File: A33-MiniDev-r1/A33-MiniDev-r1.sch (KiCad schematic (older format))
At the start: 8 parts, among them IC1 AXP223, U1 A33

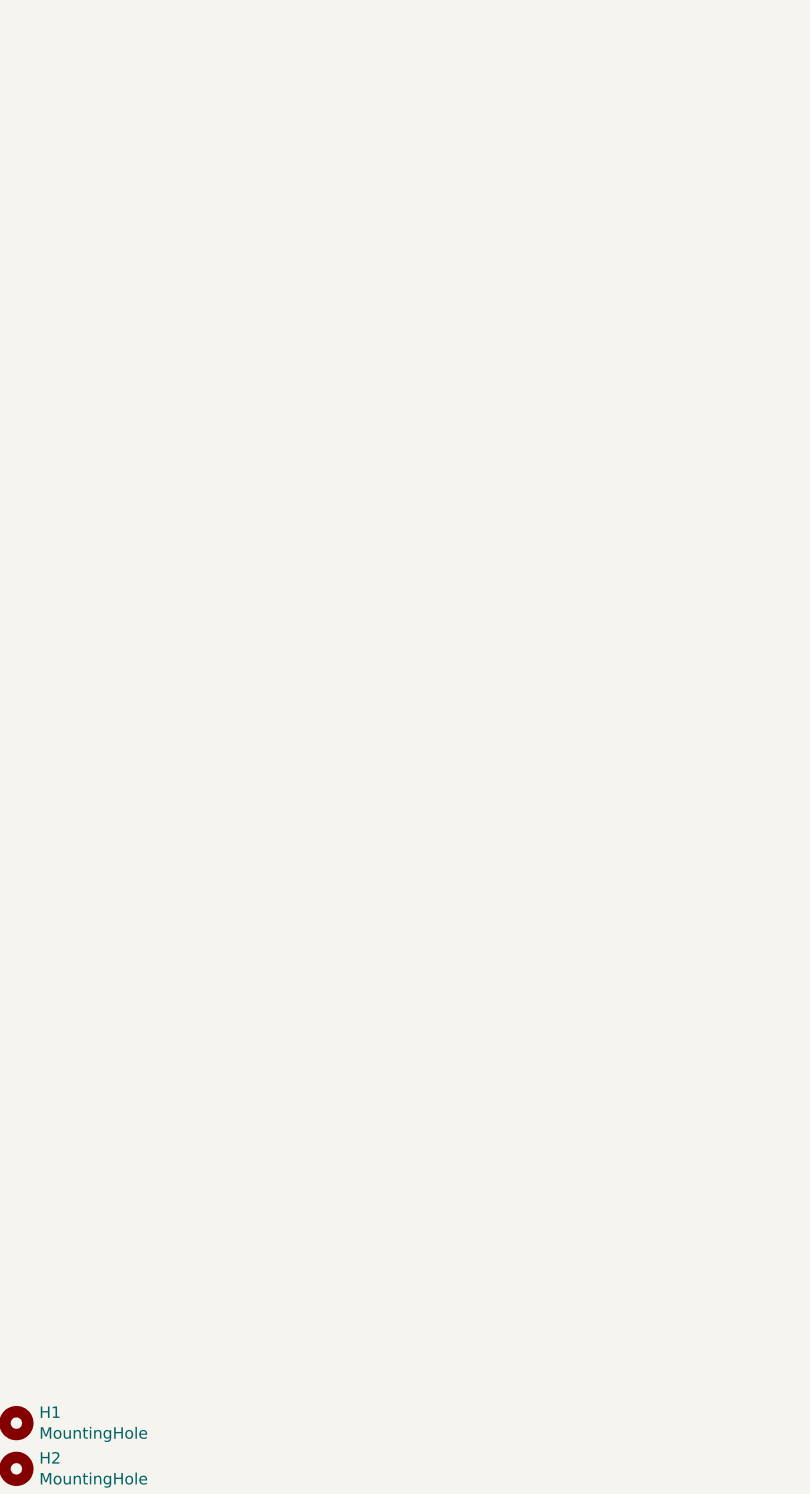
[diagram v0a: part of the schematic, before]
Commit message: Uploaded RAM chip library and placed on schematic
IS43TR16640CL-123JBLI
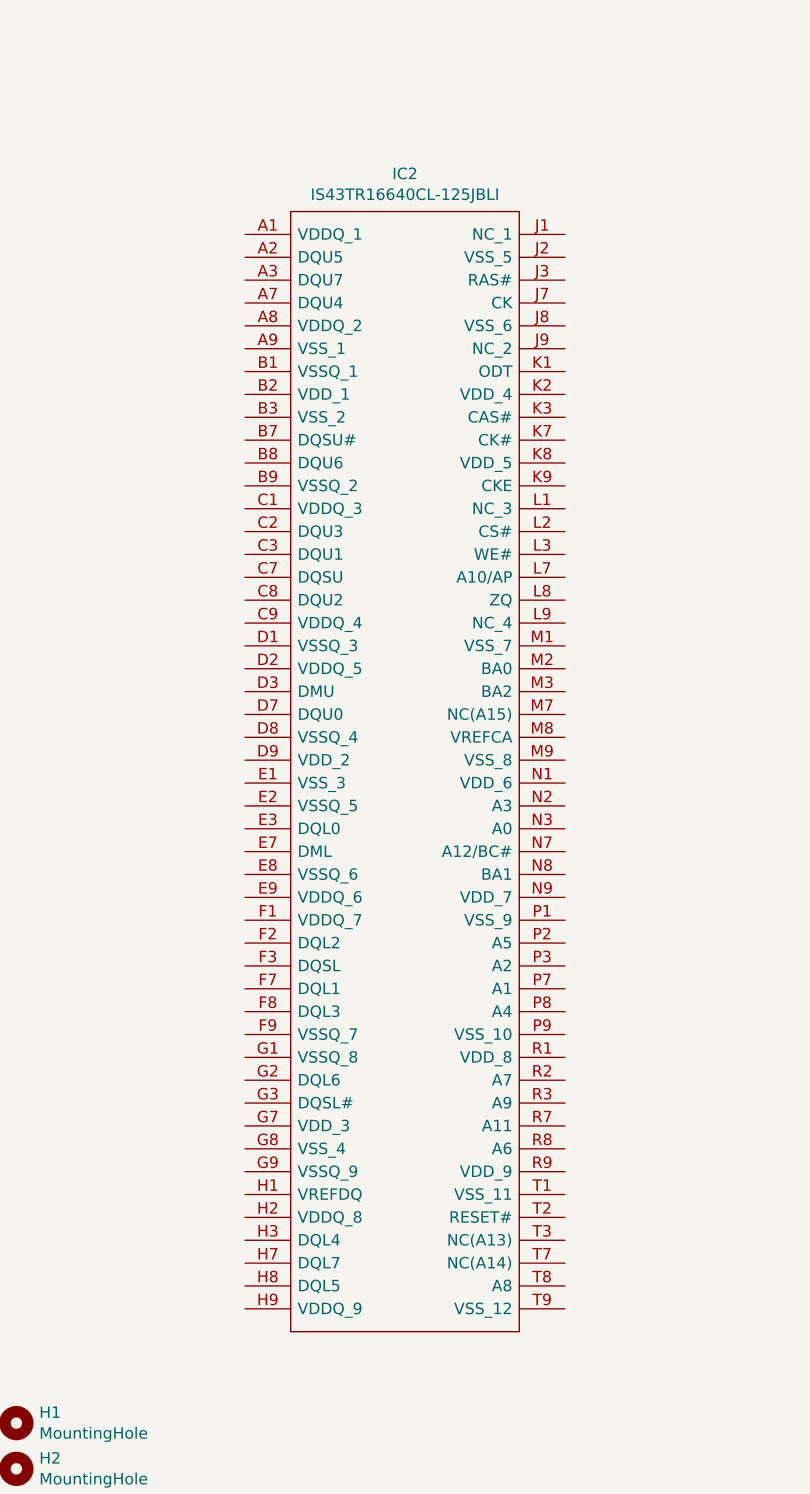
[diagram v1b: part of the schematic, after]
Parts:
- added IC2: IS43TR16640CL-125JBLI, BGA96C80P9X16_900X1300X120, symbol IS43TR16640CL-125JBLI:IS43TR16640CL-125JBLI
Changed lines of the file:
@@
 Wire Wire Line
 	16900 2100 16900 1900
-Wire Bus Line
-	3500 1600 3500 3100
 $Comp
 L power:VBUS 5V_EXT
@@
 	1    0    0    -1
 $EndComp
+Wire Bus Line
+	3500 1600 3500 3100
+$Comp
+L IS43TR16640CL-125JBLI:IS43TR16640CL-125JBLI IC2
+U 1 1 61103768
+P 2000 9800
+F 0 "IC2" H 2700 10065 50  0000 C CNN
+F 1 "IS43TR16640CL-125JBLI" H 2700 9974 50  0000 C CNN
+F 2 "BGA96C80P9X16_900X1300X120" H 3250 9900 50  0001 L CNN
+F 3 "https://www.issi.com/WW/pdf/43-46TR16640C-81280CL.pdf" H 3250 9800 50  0001 L CNN
+F 4 "DRAM 1G, 1.35V, DDR3, 64Mx16, 1600MT/s @ 10-10-10, 96 ball BGA (9mm x13mm) RoHS. IT" H 3250 9700 50  0001 L CNN "Description"
+F 5 "1.2" H 3250 9600 50  0001 L CNN "Height"
+F 6 "870-16640CL-125JBLI" H 3250 9500 50  0001 L CNN "Mouser Part Number"
+F 7 "https://www.mouser.co.uk/ProductDetail/ISSI/IS43TR16640CL-125JBLI?qs=BJlw7L4Cy7%2F%252B7noTMkJDFw%3D%3D" H 3250 9400 50  0001 L CNN "Mouser Price/Stock"
+F 8 "Integrated Silicon Solution Inc." H 3250 9300 50  0001 L CNN "Manufacturer_Name"
+F 9 "IS43TR16640CL-125JBLI" H 3250 9200 50  0001 L CNN "Manufacturer_Part_Number"
+	1    2000 9800
+	1    0    0    -1
+$EndComp

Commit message: Uploaded MOSFET; initial power connections on schematic
Caps and resistors not picked yet (hopefully in stock...) but RAM chips and MOSFETs have been ordered
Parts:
- added C? (x2): 1uF, symbol Device:C_Small
- added C?, Cx (x4): 10uF/6.3V, symbol Device:C_Small
- added Q1: CSD25310Q2T, CSD25310Q2T, symbol CSD25310Q2T:CSD25310Q2T
- added R1, R2: 22R, symbol Device:R_US
- added R3: 240R, symbol Device:R_US
- added R?: 1R, symbol Device:R_US
- added R? (x2): 0.01R, symbol Device:R_US
- gave numbers to parts that had none: 1
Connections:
- net labels added: !C5, !CAS, !CK, !CKE, !CS, !LDQS, !RAS, !RST, !UDQS, !WE, CHGLED, CHGSENSEN, CHGSENSEP, CK, LDM, LDQS, ODT, UDM, UDQS, adr0, adr1, adr10, adr11, adr12, adr13, adr14, adr15, adr2, adr3, adr4, adr5, adr6, adr7, adr8, adr9, adr[0..15], dba0, dba1, dba2, dba[0..2]
- wire segments 88 -> 217
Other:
- note added: "Cx = 10uF/6.3V"

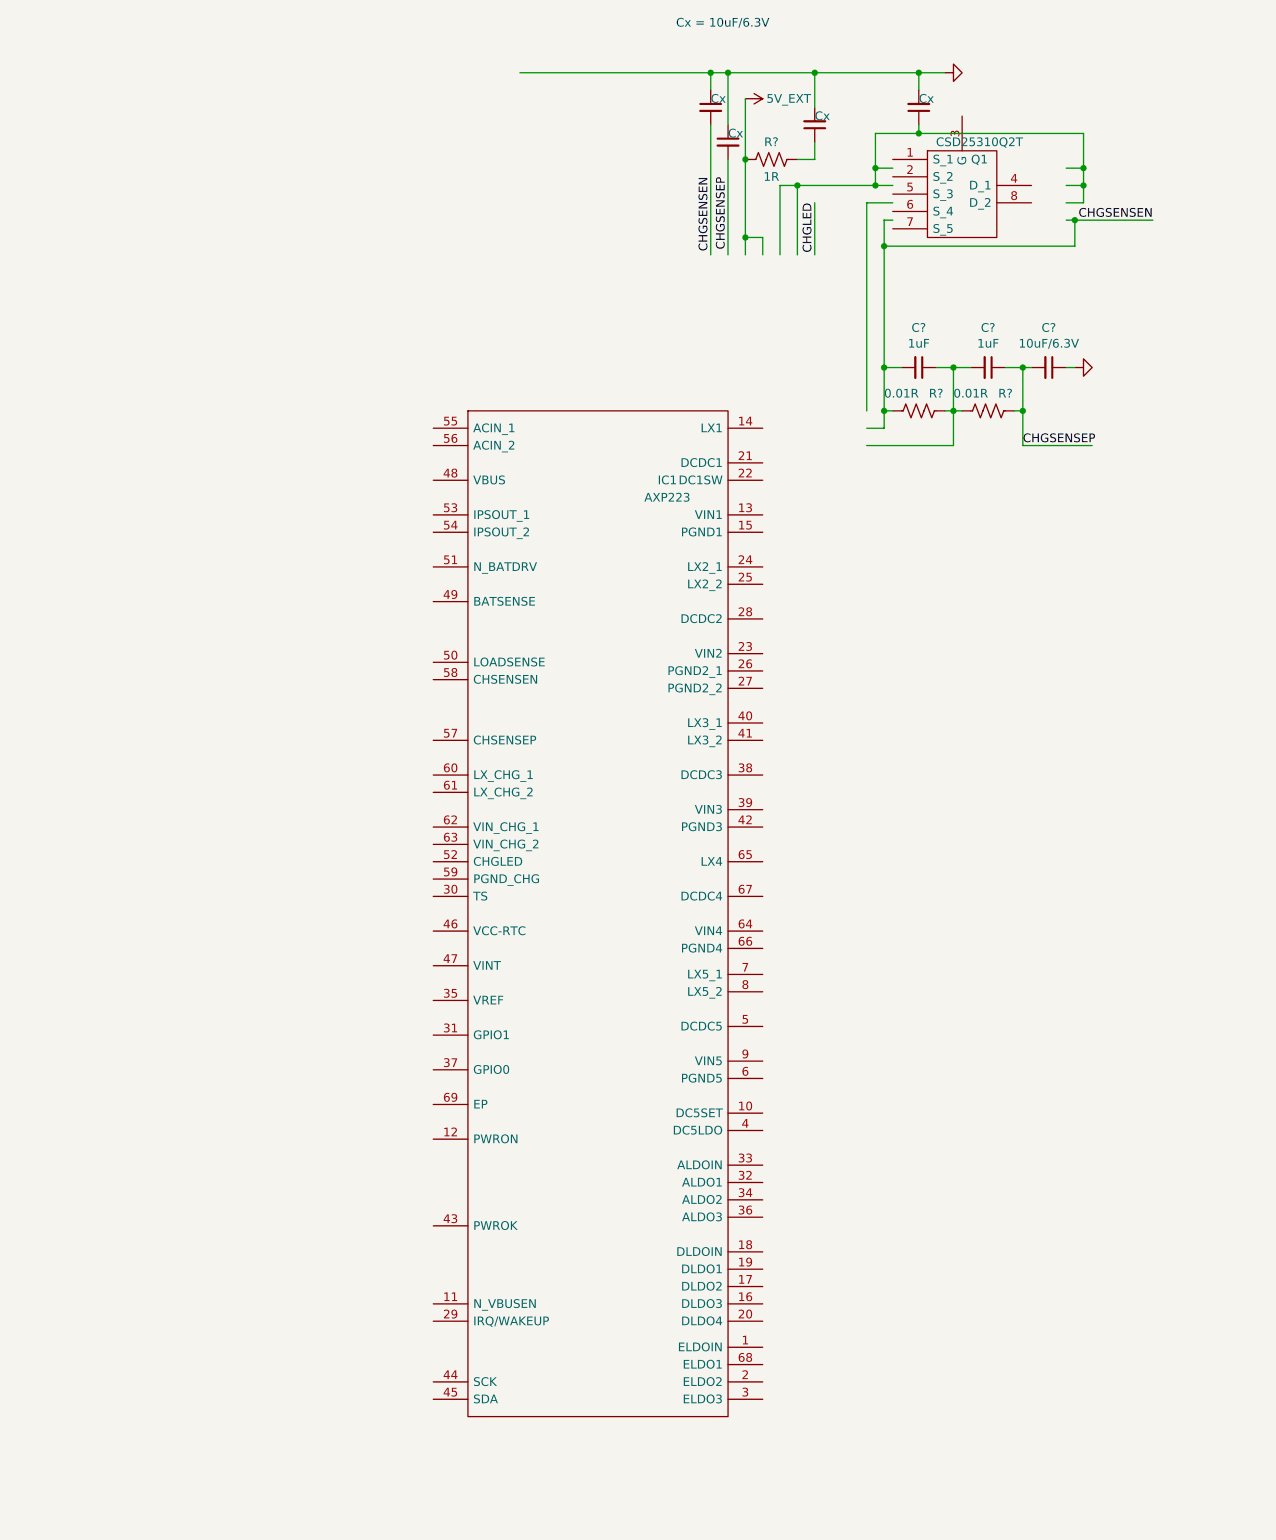
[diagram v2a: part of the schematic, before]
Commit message: Power IC placement
Redesigned schematic and part for AXP223 chip
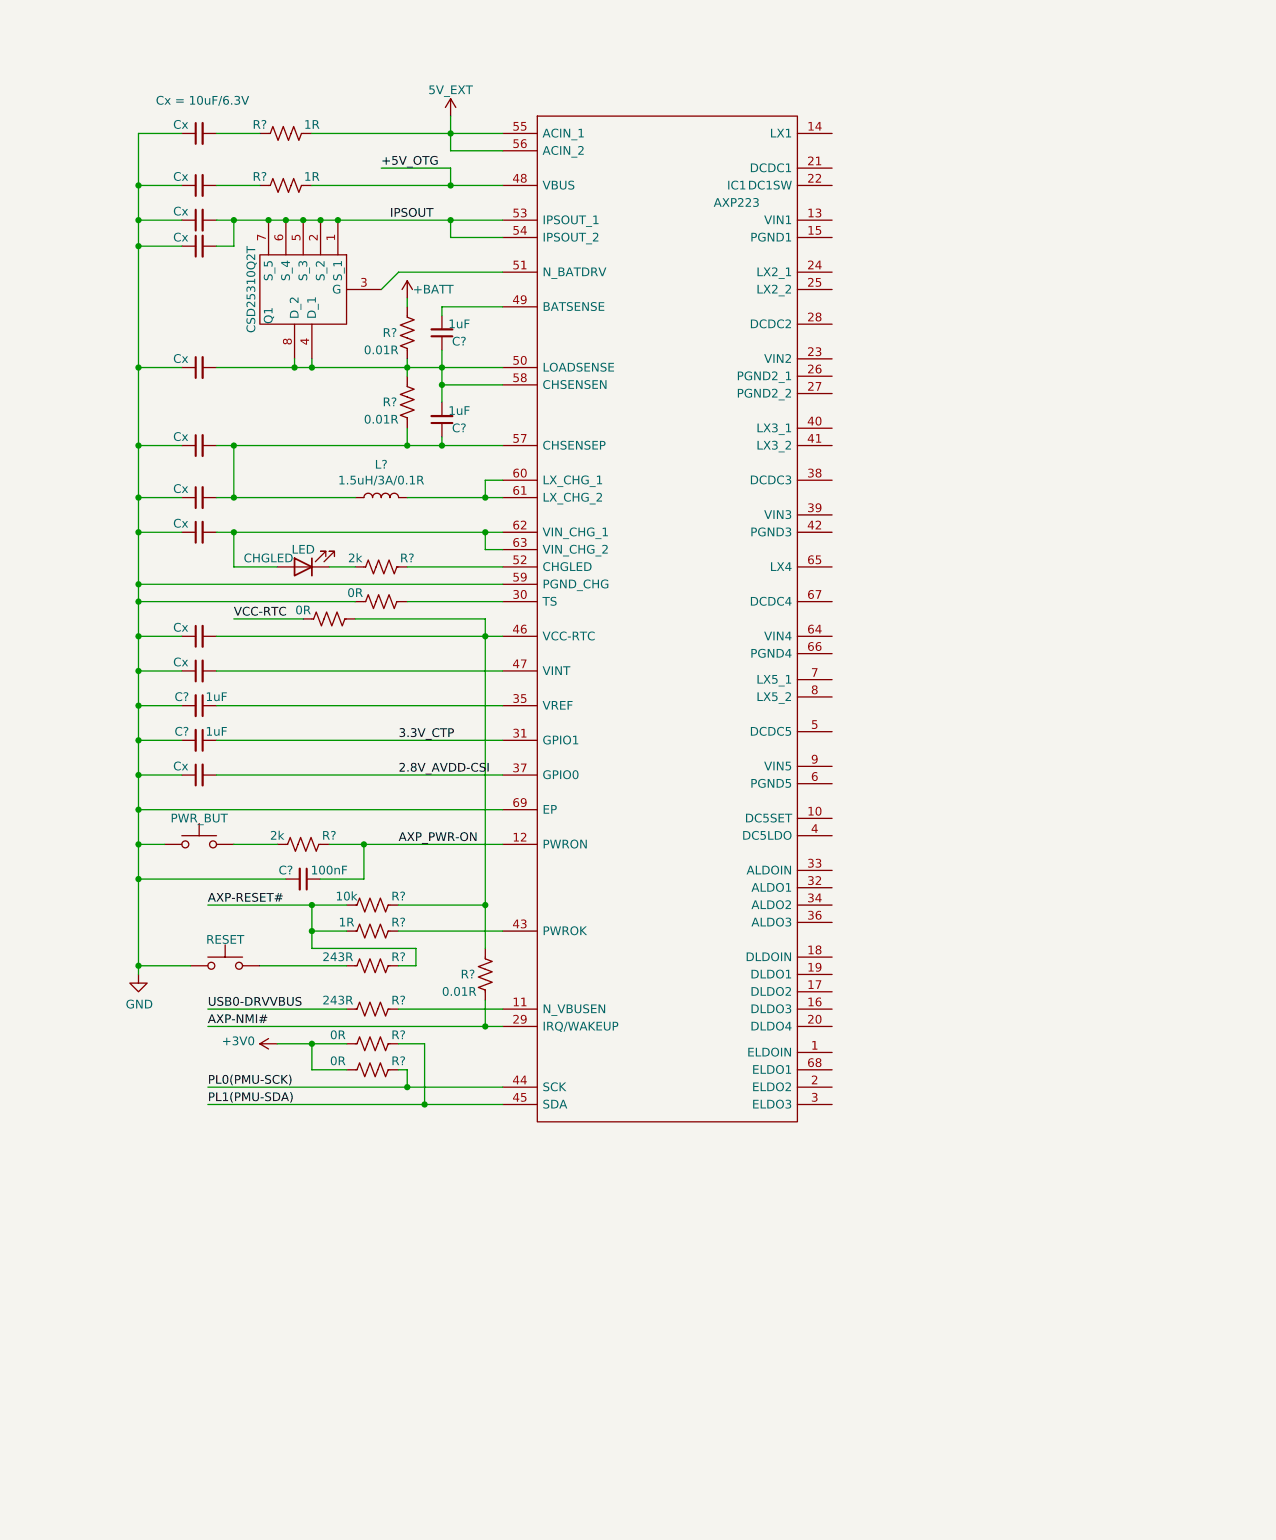
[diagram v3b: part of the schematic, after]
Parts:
- removed C?: 1uF, symbol Device:C_Small
- removed C?, Cx (x3): 10uF/6.3V, symbol Device:C_Small
- removed R?: 0.01R, symbol Device:R_US
- added C? (x3): 1uF, symbol Device:C_Small
- added C?: 100nF, symbol Device:C_Small
- added CHGLED: LED, symbol Device:LED
- added Cx (x10): 10uF/6.3V, symbol Device:C_Small
- added L?: 1.5uH/3A/0.1R, symbol Device:L
- added PWR_BUT, RESET: SW_Push, symbol Switch:SW_Push
- added R? (x2): 1R, symbol Device:R_US
- added R? (x3): 0.01R, symbol Device:R_US
- added R? (x4): 0R, symbol Device:R_US
- added R?: 2k, symbol Device:R_US
- added R?: 10k, symbol Device:R_US
- added R? (x2): 243R, symbol Device:R_US
- R?: value 0.01R -> 2k
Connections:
- net labels added: +3V0, +5V_OTG, +BATT, 2.8V_AVDD-CSI, 3.3V_CTP, AXP-NMI#, AXP-RESET#, AXP_PWR-ON, IPSOUT, PL0(PMU-SCK), PL1(PMU-SDA), USB0-DRVVBUS, VCC-RTC
- net labels removed: CHGLED, CHGSENSEN, CHGSENSEP
- wire segments 217 -> 299
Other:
- moved on the sheet: C?, Cx, IC1, Q1, R?

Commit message: Power IC updates
connected right side of schematic; new 1.1V-CPU symbol
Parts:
- added C?: 22uF/6.3V, symbol Device:C_Small
- added Cx (x24): 10uF/6.3V, symbol Device:C_Small
- added J?: Conn_01x02_Female, symbol Connector:Conn_01x02_Female
- added L? (x5): 1.5uH/3A, symbol Device:L
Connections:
- net +3V0: now also IC1.1 (ELDOIN), IC1.21 (DCDC1), Cx.1, L?.2
- net +BATT: now also C?.2, IC1.49 (BATSENSE), C?.1, J?.2 (Pin_2)
- net GND: now also IC1.10 (DC5SET), IC1.15 (PGND1), IC1.26 (PGND2_1), IC1.27 (PGND2_2), IC1.42 (PGND3), IC1.6 (PGND5), IC1.66 (PGND4), C?.2, Cx.2, Cx.2, Cx.2, Cx.2, Cx.2, Cx.2, Cx.2, Cx.2, Cx.2, Cx.2, Cx.2, Cx.2, Cx.2, Cx.2, Cx.2, Cx.2, Cx.2, Cx.2, Cx.2, Cx.2, Cx.2, Cx.2, Cx.2, Cx.2, J?.1 (Pin_1)
- net IPSOUT: now also IC1.18 (DLDOIN), IC1.23 (VIN2), IC1.33 (ALDOIN), IC1.39 (VIN3), IC1.64 (VIN4), IC1.9 (VIN5), Cx.1, Cx.1, Cx.1, Cx.1, Cx.1, Cx.1
- net at IC1.13 (VIN1): now also Cx.1
- net at IC1.14 (LX1): now also L?.1
- net DLDO3: now reaches IC1.16 (DLDO3)
- net DLDO3: now also Cx.1
- net DLDO2: now reaches IC1.17 (DLDO2)
- net DLDO2: now also Cx.1
- net DLDO1: now reaches IC1.19 (DLDO1)
- net DLDO1: now also Cx.1
- net at IC1.2 (ELDO2): now also Cx.1
- net DLDO4: now reaches IC1.20 (DLDO4)
- net DLDO4: now also Cx.1
- net VCC-LCD(3V0): now reaches IC1.22 (DC1SW)
- net VCC-LCD(3V0): now also Cx.1
- net at IC1.24 (LX2_1): now also IC1.25 (LX2_2), L?.1
- net +1V1: now reaches IC1.28 (DCDC2)
- net +1V1: now also Cx.1, L?.2
- net at IC1.3 (ELDO3): now also Cx.1
- net 3.0V_ALDO1: now reaches IC1.32 (ALDO1)
- net 3.0V_ALDO1: now also Cx.1
- net 2.5V_ALDO2: now reaches IC1.34 (ALDO2)
- net 2.5V_ALDO2: now also Cx.1
- net ALDO3: now reaches IC1.36 (ALDO3)
- net ALDO3: now also Cx.1
- net +1V1_CPU: now reaches IC1.38 (DCDC3)
- net +1V1_CPU: now also Cx.1, L?.2
- net 1.1V_CPUS: now reaches IC1.4 (DC5LDO)
- net 1.1V_CPUS: now also Cx.1
- net at IC1.40 (LX3_1): now also IC1.41 (LX3_2), L?.1
- net +1V5: now reaches IC1.5 (DCDC5)
- net +1V5: now also Cx.1, L?.2
- net at IC1.65 (LX4): now also L?.1
- net DCDC4_OUT: now reaches IC1.67 (DCDC4)
- net DCDC4_OUT: now also Cx.1, L?.2
- net at IC1.68 (ELDO1): now also Cx.1
- net at IC1.7 (LX5_1): now also IC1.8 (LX5_2), L?.1
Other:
- note added: "1.1V@100mA"
- note added: "2.5V@300mA"
- note added: "2.8V@200mA"
- note added: "3.0V@200mA"
- note added: "3.0V@300mA"
- note added: "3.3V@100mA"
- note added: "3.3V@200mA"
- note added: "3.3V@400mA"
- note added: "3V0@600mA"
- note added: "VCC-DRAM\n1.5V/1.2V@2A"
- note added: "VDD-CPU\n1.1V@2A"
- note added: "VDD-SYS\n1.1V@2A"
- moved on the sheet: U2B
